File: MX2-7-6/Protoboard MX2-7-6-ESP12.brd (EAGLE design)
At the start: 54.2 x 59.6 mm, 248 parts

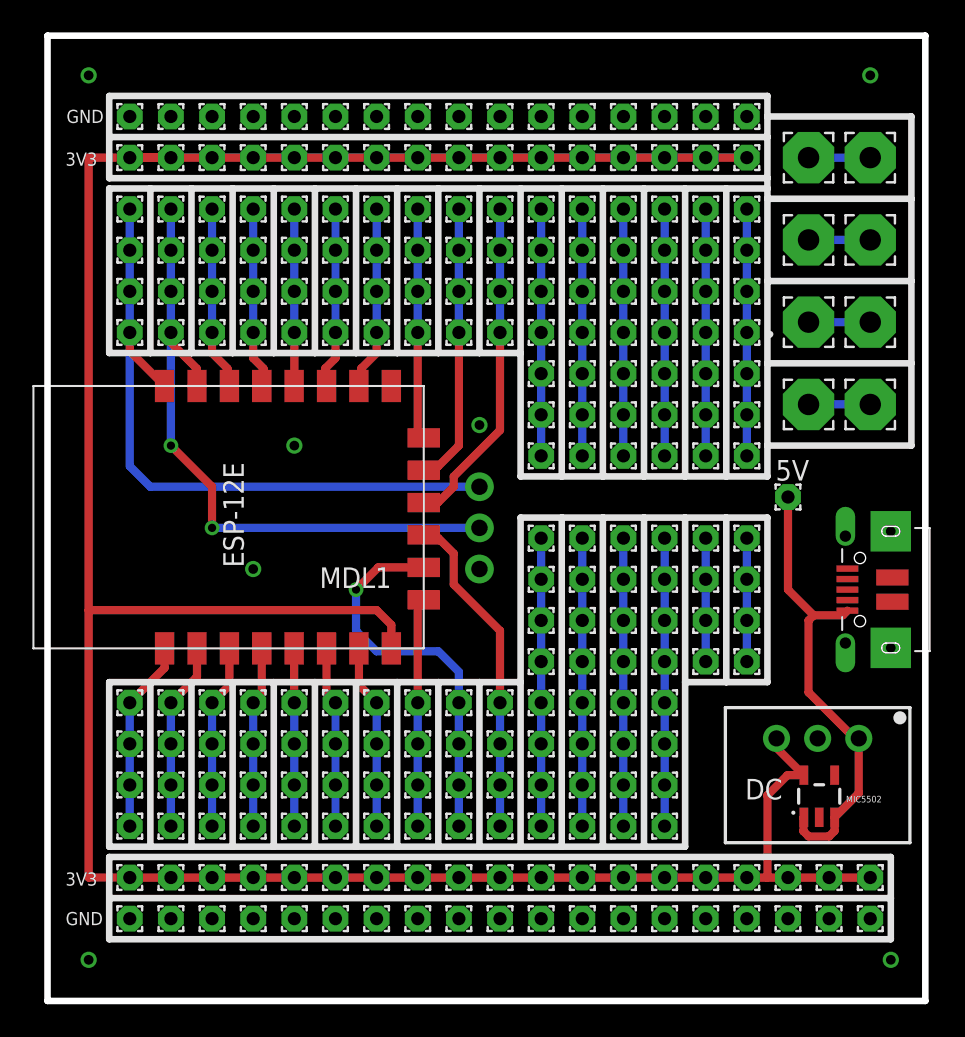
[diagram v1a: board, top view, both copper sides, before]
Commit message: Update to rev2
Updated to Pin headers instead of single wire pads
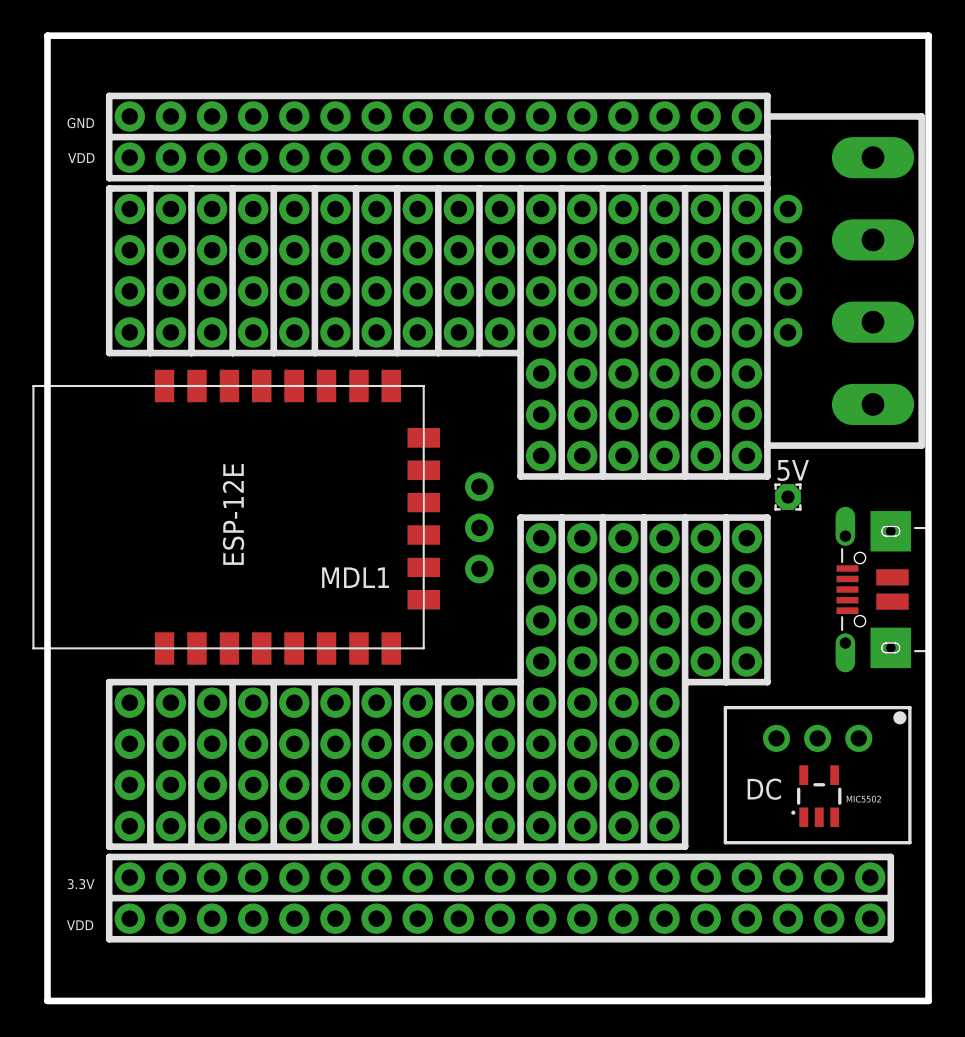
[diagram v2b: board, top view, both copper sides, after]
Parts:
- removed PAD10, PAD101, PAD102, PAD104, PAD105, PAD106, PAD107, PAD108, PAD11, PAD110, PAD112, PAD113, PAD114, PAD115, PAD116, PAD117, PAD12, PAD124, PAD125, PAD126, PAD13, PAD133, PAD134, PAD135, PAD14, PAD142, PAD143, PAD144, PAD15, PAD16, PAD169, PAD17, PAD170, PAD171, PAD172, PAD173, PAD174, PAD175, PAD178, PAD179, PAD18, PAD180, PAD181, PAD182, PAD183, PAD184, PAD187, PAD188, PAD189, PAD19, PAD190, PAD191, PAD192, PAD193, PAD196, PAD197, PAD198, PAD199, PAD20, PAD200, PAD201, PAD202, PAD205, PAD206, PAD207, PAD208, PAD209, PAD21, PAD210, PAD211, PAD214, PAD215, PAD216, PAD217, PAD218, PAD219, PAD22, PAD220, PAD23, PAD24, PAD25, PAD26, PAD269, PAD27, PAD270, PAD271, PAD272, PAD278, PAD279, PAD28, PAD280, PAD281, PAD282, PAD283, PAD284, PAD287, PAD288, PAD289, PAD29, PAD290, PAD291, PAD292, PAD293, PAD296, PAD297, PAD298, PAD299, PAD3, PAD30, PAD300, PAD301, PAD302, PAD305, PAD306, PAD307, PAD308, PAD309, PAD31, PAD310, PAD311, PAD32, PAD33, PAD36, PAD37, PAD38, PAD4, PAD41, PAD421, PAD422, PAD423, PAD424, PAD425, PAD426, PAD427, PAD428, PAD429, PAD430, PAD431, PAD432, PAD433, PAD434, PAD435, PAD436, PAD439, PAD44, PAD440, PAD441, PAD442, PAD443, PAD444, PAD445, PAD446, PAD447, PAD448, PAD449, PAD450, PAD451, PAD452, PAD453, PAD454, PAD455, PAD456, PAD459, PAD460, PAD461, PAD462, PAD48, PAD49, PAD5, PAD50, PAD52, PAD53, PAD54, PAD56, PAD57, PAD58, PAD6, PAD60, PAD61, PAD62, PAD64, PAD65, PAD66, PAD68, PAD69, PAD7, PAD70, PAD71, PAD72, PAD73, PAD74, PAD76, PAD77, PAD78, PAD79, PAD8, PAD80, PAD81, PAD83, PAD84, PAD85, PAD87, PAD88, PAD89, PAD9, PAD90, PAD92, PAD93, PAD96, PAD97, PAD98, PAD99: (no value), wirepad:1,6/0,8
- removed PAD100: 5, wirepad:1,6/0,8
- removed PAD103: SO, wirepad:1,6/0,8
- removed PAD109: 4, wirepad:1,6/0,8
- removed PAD111: 9, wirepad:1,6/0,8
- removed PAD118: 0, wirepad:1,6/0,8
- removed PAD127: 2, wirepad:1,6/0,8
- removed PAD136: 15, wirepad:1,6/0,8
- removed PAD145: SC, wirepad:1,6/0,8
- removed PAD34, PAD35, PAD39, PAD40, PAD42, PAD43, PAD45, PAD46: (no value), wirepad:3,17/1,3
- removed PAD47: AC, wirepad:1,6/0,8
- removed PAD51: CH, wirepad:1,6/0,8
- removed PAD55: 16, wirepad:1,6/0,8
- removed PAD59: 14, wirepad:1,6/0,8
- removed PAD63: 12, wirepad:1,6/0,8
- removed PAD67: 13, wirepad:1,6/0,8
- removed PAD75: CS, wirepad:1,6/0,8
- removed PAD82: TX, wirepad:1,6/0,8
- removed PAD86: SI, wirepad:1,6/0,8
- removed PAD91: RX, wirepad:1,6/0,8
- removed PAD94: 10, wirepad:1,6/0,8
- removed PAD95: RS, wirepad:1,6/0,8
- added 3.3V, VDD: (no value), SparkFun-Connectors:1X19_NO_SILK
- added GND, J33: (no value), SparkFun-Connectors:1X16_NO_SILK
- added J1, J10, J11, J12, J13, J14, J15, J16, J17, J18, J19, J2, J20, J3, J31, J32, J4, J5, J6, J7, J8, J9: (no value), SparkFun-Connectors:1X04_NO_SILK_ALL_ROUND
- added J21, J22, J23, J24, J25, J26: (no value), SparkFun-Connectors:1X07_NO_SILK
- added J27, J28, J29, J30: (no value), SparkFun-Connectors:1X08_NO_SILK
- added JP1, JP2, JP6, JP7: (no value), adafruit:1X1-BIGPOGO
- added JP10, JP11, JP8, JP9: (no value), adafruit:1X01-CLEANBIG
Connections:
- removed net N$2: PAD34.1, PAD35.1
- removed net N$38: MDL1.21, PAD83.1, PAD84.1, PAD85.1, PAD86.1
- removed net N$39: MDL1.20, PAD87.1, PAD92.1, PAD93.1, PAD94.1
- removed net N$4: PAD39.1, PAD40.1
- removed net N$42: MDL1.19, PAD111.1, PAD112.1, PAD113.1, PAD114.1
- removed net N$5: PAD42.1, PAD43.1
- removed net N$53: MDL1.4, PAD55.1, PAD56.1, PAD57.1, PAD58.1
- removed net N$58: MDL1.18, PAD103.1, PAD104.1, PAD105.1, PAD110.1
- removed net N$6: PAD45.1, PAD46.1
- new net N$15: J10.1, J10.2, J10.3, J10.4
- new net N$16: J18.1, J18.2, J18.3, J18.4
- new net N$23: J19.1, J19.2, J19.3, J19.4
- new net N$24: J20.1, J20.2, J20.3, J20.4
- new net N$25: J28.1, J28.2, J28.3, J28.4, J28.5, J28.6, J28.7, J28.8
- new net N$27: J29.1, J29.2, J29.3, J29.4, J29.5, J29.6, J29.7, J29.8
- new net N$3: J8.1, J8.2, J8.3, J8.4
- new net N$33: JP10.1, JP6.P$1
- new net N$34: J17.1, J17.2, J17.3, J17.4
- new net N$7: J1.1, J1.2, J1.3, J1.4
- new net N$8: J2.1, J2.2, J2.3, J2.4
- net GND: now also GND.1, GND.10, GND.11, GND.12, GND.13, GND.14, GND.15, GND.16, GND.2, GND.3, GND.4, GND.5, GND.6, GND.7, GND.8, GND.9, VDD.1, VDD.10, VDD.11, VDD.12, VDD.13, VDD.14, VDD.15, VDD.16, VDD.17, VDD.18, VDD.19, VDD.2, VDD.3, VDD.4, VDD.5, VDD.6, VDD.7, VDD.8, VDD.9; no longer PAD17.1, PAD22.1, PAD23.1, PAD24.1, PAD25.1, PAD26.1, PAD27.1, PAD28.1, PAD29.1, PAD30.1, PAD31.1, PAD32.1, PAD33.1, PAD36.1, PAD38.1, PAD4.1, PAD421.1, PAD422.1, PAD423.1, PAD424.1, PAD425.1, PAD426.1, PAD427.1, PAD428.1, PAD429.1, PAD430.1, PAD431.1, PAD432.1, PAD433.1, PAD434.1, PAD435.1, PAD436.1, PAD439.1, PAD440.1, PAD441.1
- net N$1: now also J21.1, J21.2, J21.3, J21.4, J21.5, J21.6, J21.7; no longer PAD3.1, PAD37.1, PAD41.1, PAD44.1
- net N$10: now also J4.1, J4.2, J4.3, J4.4; no longer PAD106.1, PAD107.1, PAD108.1, PAD109.1
- net N$11: now also J5.1, J5.2, J5.3, J5.4; no longer PAD115.1, PAD116.1, PAD117.1, PAD118.1
- net N$12: now also J6.1, J6.2, J6.3, J6.4; no longer PAD124.1, PAD125.1, PAD126.1, PAD127.1
- net N$13: now also J7.1, J7.2, J7.3, J7.4; no longer PAD133.1, PAD134.1, PAD135.1, PAD136.1
- net N$14: now also J9.1, J9.2, J9.3, J9.4; no longer MDL1.22, PAD142.1, PAD143.1, PAD144.1, PAD145.1
- net N$17: now also J22.1, J22.2, J22.3, J22.4, J22.5, J22.6, J22.7; no longer PAD169.1, PAD170.1, PAD171.1, PAD172.1, PAD173.1, PAD174.1, PAD175.1
- net N$18: now also J23.1, J23.2, J23.3, J23.4, J23.5, J23.6, J23.7; no longer PAD178.1, PAD179.1, PAD180.1, PAD181.1, PAD182.1, PAD183.1, PAD184.1
- net N$19: now also J24.1, J24.2, J24.3, J24.4, J24.5, J24.6, J24.7; no longer PAD187.1, PAD188.1, PAD189.1, PAD190.1, PAD191.1, PAD192.1, PAD193.1
- net N$20: now also J25.1, J25.2, J25.3, J25.4, J25.5, J25.6, J25.7; no longer PAD196.1, PAD197.1, PAD198.1, PAD199.1, PAD200.1, PAD201.1, PAD202.1
- net N$21: now also J26.1, J26.2, J26.3, J26.4, J26.5, J26.6, J26.7; no longer PAD205.1, PAD206.1, PAD207.1, PAD208.1, PAD209.1, PAD210.1, PAD211.1
- net N$22: now also J27.1, J27.2, J27.3, J27.4, J27.5, J27.6, J27.7, J27.8; no longer PAD214.1, PAD215.1, PAD216.1, PAD217.1, PAD218.1, PAD219.1, PAD220.1
- net N$26: now also J14.1, J14.2, J14.3, J14.4; no longer PAD59.1, PAD60.1, PAD61.1, PAD62.1
- net N$28: now also J30.1, J30.2, J30.3, J30.4, J30.5, J30.6, J30.7, J30.8; no longer PAD269.1, PAD270.1, PAD271.1, PAD272.1
- net N$29: now also J31.1, J31.2, J31.3, J31.4; no longer PAD278.1, PAD279.1, PAD280.1, PAD281.1, PAD282.1, PAD283.1, PAD284.1, PAD71.1
- net N$30: now also J32.1, J32.2, J32.3, J32.4; no longer PAD287.1, PAD288.1, PAD289.1, PAD290.1, PAD291.1, PAD292.1, PAD293.1, PAD72.1
- net N$31: now also JP1.P$1, JP8.1; no longer PAD296.1, PAD297.1, PAD298.1, PAD299.1, PAD300.1, PAD301.1, PAD302.1, PAD73.1
- net N$32: now also JP2.P$1, JP9.1; no longer PAD305.1, PAD306.1, PAD307.1, PAD308.1, PAD309.1, PAD310.1, PAD311.1, PAD74.1
- net N$35: now also JP11.1, JP7.P$1; no longer MDL1.17, PAD75.1, PAD76.1, PAD77.1, PAD78.1
- net N$50: now also J11.1, J11.2, J11.3, J11.4; no longer PAD101.1, PAD102.1, PAD95.1, PAD96.1
- net N$51: now also J12.1, J12.2, J12.3, J12.4; no longer PAD47.1, PAD48.1, PAD49.1, PAD50.1
- net N$52: now also J13.1, J13.2, J13.3, J13.4; no longer PAD51.1, PAD52.1, PAD53.1, PAD54.1
- net N$55: now also J15.1, J15.2, J15.3, J15.4; no longer PAD63.1, PAD64.1, PAD65.1, PAD66.1
- net N$56: now also J16.1, J16.2, J16.3, J16.4; no longer PAD67.1, PAD68.1, PAD69.1, PAD70.1
- net N$9: now also J3.1, J3.2, J3.3, J3.4; no longer PAD100.1, PAD97.1, PAD98.1, PAD99.1
- net RX: no longer PAD88.1, PAD89.1, PAD90.1, PAD91.1
- net TX: no longer PAD79.1, PAD80.1, PAD81.1, PAD82.1
- net VDD: now also 3.3V.1, 3.3V.10, 3.3V.11, 3.3V.12, 3.3V.13, 3.3V.14, 3.3V.15, 3.3V.16, 3.3V.17, 3.3V.18, 3.3V.19, 3.3V.2, 3.3V.3, 3.3V.4, 3.3V.5, 3.3V.6, 3.3V.7, 3.3V.8, 3.3V.9, J33.1, J33.10, J33.11, J33.12, J33.13, J33.14, J33.15, J33.16, J33.2, J33.3, J33.4, J33.5, J33.6, J33.7, J33.8, J33.9; no longer PAD10.1, PAD11.1, PAD12.1, PAD13.1, PAD14.1, PAD15.1, PAD16.1, PAD18.1, PAD19.1, PAD20.1, PAD21.1, PAD442.1, PAD443.1, PAD444.1, PAD445.1, PAD446.1, PAD447.1, PAD448.1, PAD449.1, PAD450.1, PAD451.1, PAD452.1, PAD453.1, PAD454.1, PAD455.1, PAD456.1, PAD459.1, PAD460.1, PAD461.1, PAD462.1, PAD5.1, PAD6.1, PAD7.1, PAD8.1, PAD9.1
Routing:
- net VDD: track 263.6 -> 0.00 mm
- net TX: track 42.8 -> 0.00 mm
- net RX: track 42.2 -> 0.00 mm, vias 2 -> 0
- net VCC: track 28.7 -> 0.00 mm
- net N$58: track 25.2 -> 0.00 mm, vias 1 -> 0
- net N$39: track 21.4 -> 0.00 mm
- net N$42: track 21.2 -> 0.00 mm
- net N$29: track 19.6 -> 0.00 mm
- net N$32: track 19.2 -> 0.00 mm
- net N$30: track 19.2 -> 0.00 mm
- net N$38: track 18.4 -> 0.00 mm
- net N$31: track 17.8 -> 0.00 mm
- net N$21: track 17.7 -> 0.00 mm
- net N$18: track 16.9 -> 0.00 mm
- net N$22: track 16.9 -> 0.00 mm
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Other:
- board size 54.2 x 59.6 mm -> 54.4 x 59.6 mm
- board text added: "VDD"
- board text removed: "3V3"
- board text removed: "GND"

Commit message: Change usb connector
Change to correct usb connecter and moved esp8266 bit more onto the
board.
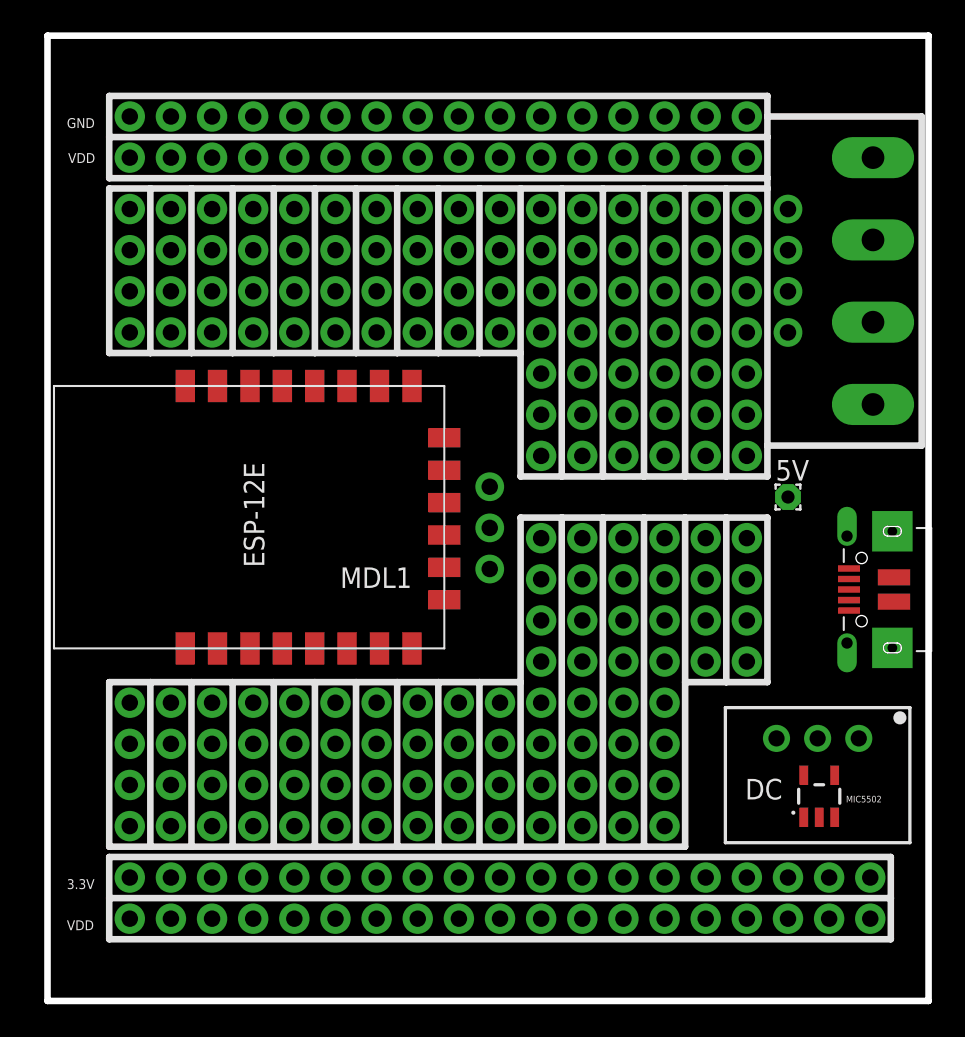
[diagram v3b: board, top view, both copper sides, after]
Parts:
- moved MDL1 1.27 mm to (14.3, 29.4)
- moved JP3 0.63 mm to (27.3, 31.8)
- moved JP4 0.63 mm to (27.3, 29.2)
- moved JP5 0.63 mm to (27.3, 26.7)
- moved X2 0.10 mm to (50.3, 25.4)
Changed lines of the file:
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@@
 <attribute name="NAME" x="43.0758625" y="12.441459375" size="1.27" layer="25"/>
 </element>
-<element name="JP3" library="adafruit" package="1X01-CLEANBIG" value="TX" x="26.67" y="31.75" smashed="yes">
-<attribute name="VALUE" x="28.57" y="31.205" size="0.6096" layer="27" rot="R90"/>
-</element>
-<element name="JP4" library="adafruit" package="1X01-CLEANBIG" value="RX" x="26.67" y="29.21" smashed="yes">
-<attribute name="VALUE" x="28.55" y="28.765" size="0.6096" layer="27" rot="R90"/>
-</element>
-<element name="JP5" library="adafruit" package="1X01-CLEANBIG" value="GND" x="26.67" y="26.67" smashed="yes">
-<attribute name="VALUE" x="28.58" y="25.775" size="0.6096" layer="27" rot="R90"/>
-</element>
-<element name="X2" library="microbuilder" package="4UCONN_20329" value="" x="50.165" y="25.4" smashed="yes" rot="R90">
-<attribute name="VALUE" x="56.575" y="22.622" size="0.4064" layer="27" ratio="10" rot="R90"/>
-</element>
-<element name="MDL1" library="ESP8266-ESP12E" package="ESP8266-ESP12E" value="" x="13.07" y="29.39" smashed="yes" rot="R90">
-<attribute name="NAME" x="21.23" y="26.77" size="1.27" layer="21" rot="R180"/>
+<element name="JP3" library="adafruit" package="1X01-CLEANBIG" value="TX" x="27.305" y="31.75" smashed="yes">
+<attribute name="VALUE" x="28.57" y="30.57" size="0.3048" layer="27" rot="R90"/>
+</element>
+<element name="JP4" library="adafruit" package="1X01-CLEANBIG" value="RX" x="27.305" y="29.21" smashed="yes">
+<attribute name="VALUE" x="28.55" y="28.13" size="0.3048" layer="27" rot="R90"/>
+</element>
+<element name="JP5" library="adafruit" package="1X01-CLEANBIG" value="GND" x="27.305" y="26.67" smashed="yes">
+<attribute name="VALUE" x="28.58" y="25.14" size="0.3048" layer="27" rot="R90"/>
+</element>
+<element name="X2" library="microbuilder" package="4UCONN_20329" value="" x="50.265" y="25.4" smashed="yes" rot="R90">
+<attribute name="VALUE" x="56.675" y="22.622" size="0.4064" layer="27" ratio="10" rot="R90"/>
+</element>
+<element name="MDL1" library="ESP8266-ESP12E" package="ESP8266-ESP12E" value="" x="14.34" y="29.39" smashed="yes" rot="R90">
+<attribute name="NAME" x="22.5" y="26.77" size="1.27" layer="21" rot="R180"/>
 </element>
 <element name="MIC5502" library="SparkFun-PowerIC" package="SOT23-5" value="" x="47.65" y="12.64" smashed="yes">
@@
 <wire x1="5.08" y1="43.815" x2="5.08" y2="46.355" width="0" layer="19" extent="1-1"/>
 <wire x1="5.08" y1="41.275" x2="5.08" y2="43.815" width="0" layer="19" extent="1-1"/>
-<wire x1="11.23" y1="37.97" x2="5.08" y2="41.275" width="0" layer="19" extent="1-1"/>
+<wire x1="12.5" y1="37.97" x2="5.08" y2="41.275" width="0" layer="19" extent="1-1"/>
 </signal>
 <signal name="N$10">
@@
 <wire x1="7.62" y1="43.815" x2="7.62" y2="46.355" width="0" layer="19" extent="1-1"/>
 <wire x1="7.62" y1="41.275" x2="7.62" y2="43.815" width="0" layer="19" extent="1-1"/>
-<wire x1="13.23" y1="37.97" x2="7.62" y2="41.275" width="0" layer="19" extent="1-1"/>
+<wire x1="14.5" y1="37.97" x2="7.62" y2="41.275" width="0" layer="19" extent="1-1"/>
 </signal>
 <signal name="N$11">
@@
 <wire x1="10.16" y1="43.815" x2="10.16" y2="46.355" width="0" layer="19" extent="1-1"/>
 <wire x1="10.16" y1="41.275" x2="10.16" y2="43.815" width="0" layer="19" extent="1-1"/>
-<wire x1="15.23" y1="37.97" x2="10.16" y2="41.275" width="0" layer="19" extent="1-1"/>
+<wire x1="16.5" y1="37.97" x2="10.16" y2="41.275" width="0" layer="19" extent="1-1"/>
 </signal>
 <signal name="N$12">
@@
 <wire x1="12.7" y1="43.815" x2="12.7" y2="46.355" width="0" layer="19" extent="1-1"/>
 <wire x1="12.7" y1="41.275" x2="12.7" y2="43.815" width="0" layer="19" extent="1-1"/>
-<wire x1="17.23" y1="37.97" x2="12.7" y2="41.275" width="0" layer="19" extent="1-1"/>
+<wire x1="18.5" y1="37.97" x2="12.7" y2="41.275" width="0" layer="19" extent="1-1"/>
 </signal>
 <signal name="N$13">
@@
 <wire x1="15.24" y1="43.815" x2="15.24" y2="46.355" width="0" layer="19" extent="1-1"/>
 <wire x1="15.24" y1="41.275" x2="15.24" y2="43.815" width="0" layer="19" extent="1-1"/>
-<wire x1="19.23" y1="37.97" x2="15.24" y2="41.275" width="0" layer="19" extent="1-1"/>
+<wire x1="20.5" y1="37.97" x2="15.24" y2="41.275" width="0" layer="19" extent="1-1"/>
 </signal>
 <signal name="GND">
@@
 <contactref element="MIC5502" pad="3"/>
 <contactref element="5V" pad="1"/>
-<wire x1="49.39" y1="24.1" x2="45.72" y2="31.115" width="0" layer="19" extent="1-1"/>
-<wire x1="50.0908625" y1="16.211459375" x2="49.39" y2="24.1" width="0" layer="19" extent="1-1"/>
+<wire x1="49.49" y1="24.1" x2="45.72" y2="31.115" width="0" layer="19" extent="1-1"/>
+<wire x1="50.0908625" y1="16.211459375" x2="49.49" y2="24.1" width="0" layer="19" extent="1-1"/>
 <wire x1="48.6" y1="11.3399" x2="50.0908625" y2="16.211459375" width="0" layer="19" extent="1-1"/>
 <wire x1="46.7" y1="11.3399" x2="48.6" y2="11.3399" width="0" layer="19" extent="1-1"/>
@@
 <wire x1="7.62" y1="52.07" x2="10.16" y2="52.07" width="0" layer="19" extent="1-1"/>
 <wire x1="5.08" y1="52.07" x2="7.62" y2="52.07" width="0" layer="19" extent="1-1"/>
-<wire x1="21.23" y1="21.77" x2="20.32" y2="52.07" width="0" layer="19" extent="1-1"/>
-<wire x1="20.32" y1="7.62" x2="21.23" y2="21.77" width="0" layer="19" extent="1-1"/>
+<wire x1="22.5" y1="21.77" x2="20.32" y2="52.07" width="0" layer="19" extent="1-1"/>
+<wire x1="20.32" y1="7.62" x2="22.5" y2="21.77" width="0" layer="19" extent="1-1"/>
 <wire x1="22.86" y1="7.62" x2="20.32" y2="7.62" width="0" layer="19" extent="1-1"/>
 <wire x1="25.4" y1="7.62" x2="22.86" y2="7.62" width="0" layer="19" extent="1-1"/>
@@
 <contactref element="J14" pad="2"/>
 <contactref element="J14" pad="1"/>
-<wire x1="12.7" y1="18.415" x2="15.23" y2="21.77" width="0" layer="19" extent="1-1"/>
+<wire x1="12.7" y1="18.415" x2="16.5" y2="21.77" width="0" layer="19" extent="1-1"/>
 <wire x1="12.7" y1="15.875" x2="12.7" y2="18.415" width="0" layer="19" extent="1-1"/>
 <wire x1="12.7" y1="13.335" x2="12.7" y2="15.875" width="0" layer="19" extent="1-1"/>
@@
 <contactref element="J11" pad="2"/>
 <contactref element="J11" pad="1"/>
-<wire x1="5.08" y1="18.415" x2="7.23" y2="21.77" width="0" layer="19" extent="1-1"/>
+<wire x1="5.08" y1="18.415" x2="8.5" y2="21.77" width="0" layer="19" extent="1-1"/>
 <wire x1="5.08" y1="15.875" x2="5.08" y2="18.415" width="0" layer="19" extent="1-1"/>
 <wire x1="5.08" y1="13.335" x2="5.08" y2="15.875" width="0" layer="19" extent="1-1"/>
@@
 <contactref element="J12" pad="2"/>
 <contactref element="J12" pad="1"/>
-<wire x1="7.62" y1="18.415" x2="9.23" y2="21.77" width="0" layer="19" extent="1-1"/>
+<wire x1="7.62" y1="18.415" x2="10.5" y2="21.77" width="0" layer="19" extent="1-1"/>
 <wire x1="7.62" y1="15.875" x2="7.62" y2="18.415" width="0" layer="19" extent="1-1"/>
 <wire x1="7.62" y1="13.335" x2="7.62" y2="15.875" width="0" layer="19" extent="1-1"/>
@@
 <contactref element="J13" pad="2"/>
 <contactref element="J13" pad="1"/>
-<wire x1="10.16" y1="18.415" x2="11.23" y2="21.77" width="0" layer="19" extent="1-1"/>
+<wire x1="10.16" y1="18.415" x2="12.5" y2="21.77" width="0" layer="19" extent="1-1"/>
 <wire x1="10.16" y1="15.875" x2="10.16" y2="18.415" width="0" layer="19" extent="1-1"/>
 <wire x1="10.16" y1="13.335" x2="10.16" y2="15.875" width="0" layer="19" extent="1-1"/>
@@
 <contactref element="J15" pad="3"/>
 <contactref element="J15" pad="4"/>
-<wire x1="15.24" y1="18.415" x2="17.23" y2="21.77" width="0" layer="19" extent="1-1"/>
+<wire x1="15.24" y1="18.415" x2="18.5" y2="21.77" width="0" layer="19" extent="1-1"/>
 <wire x1="15.24" y1="15.875" x2="15.24" y2="18.415" width="0" layer="19" extent="1-1"/>
 <wire x1="15.24" y1="13.335" x2="15.24" y2="15.875" width="0" layer="19" extent="1-1"/>
@@
 <contactref element="J16" pad="3"/>
 <contactref element="J16" pad="4"/>
-<wire x1="17.78" y1="18.415" x2="19.23" y2="21.77" width="0" layer="19" extent="1-1"/>
+<wire x1="17.78" y1="18.415" x2="20.5" y2="21.77" width="0" layer="19" extent="1-1"/>
 <wire x1="17.78" y1="15.875" x2="17.78" y2="18.415" width="0" layer="19" extent="1-1"/>
 <wire x1="17.78" y1="13.335" x2="17.78" y2="15.875" width="0" layer="19" extent="1-1"/>
@@
 <contactref element="MDL1" pad="16"/>
 <contactref element="JP3" pad="1"/>
-<wire x1="7.23" y1="37.97" x2="26.67" y2="31.75" width="0" layer="19" extent="1-1"/>
+<wire x1="8.5" y1="37.97" x2="27.305" y2="31.75" width="0" layer="19" extent="1-1"/>
 </signal>
 <signal name="RX">
 <contactref element="MDL1" pad="15"/>
 <contactref element="JP4" pad="1"/>
-<wire x1="9.23" y1="37.97" x2="26.67" y2="29.21" width="0" layer="19" extent="1-1"/>
+<wire x1="10.5" y1="37.97" x2="27.305" y2="29.21" width="0" layer="19" extent="1-1"/>
 </signal>
 <signal name="N$3">

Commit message: Change ESP Module
Changed to Device/Package Adafruit uses
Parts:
- removed MDL1: (no value), ESP8266-ESP12E:ESP8266-ESP12E
- added X1: ESP-12E, microbuilder:ESP-12E
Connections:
- removed net N$26: J14.1, J14.2, J14.3, J14.4, MDL1.5
- removed net N$55: J15.1, J15.2, J15.3, J15.4, MDL1.6
- removed net N$56: J16.1, J16.2, J16.3, J16.4, MDL1.7
- new net N$2: J16.1, J16.2, J16.3, J16.4, X1.6
- new net N$36: J14.1, J14.2, J14.3, J14.4, X1.4
- new net N$6: J15.1, J15.2, J15.3, J15.4, X1.5
- net GND: now also X1.9; no longer MDL1.9
- net N$10: now also X1.13; no longer MDL1.13
- net N$11: now also X1.12; no longer MDL1.12
- net N$12: now also X1.11; no longer MDL1.11
- net N$13: now also X1.10; no longer MDL1.10
- net N$34: now also X1.7
- net N$50: now also X1.1; no longer MDL1.1
- net N$51: now also X1.2; no longer MDL1.2
- net N$52: now also X1.3; no longer MDL1.3
- net N$9: now also X1.14; no longer MDL1.14
- net RX: now also X1.15; no longer MDL1.15
- net TX: now also X1.16; no longer MDL1.16
- net VDD: now also X1.8; no longer MDL1.8

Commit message: Update esp component and usb
test
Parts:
- moved 5V 2.54 mm to (45.7, 28.6)
- moved JP1 1.91 mm to (51.0, 50.2)
- moved JP10 1.91 mm to (45.7, 41.9)
- moved JP11 1.91 mm to (45.7, 39.4)
- moved JP2 1.91 mm to (51.0, 45.1)
- moved JP7 1.91 mm to (51.0, 34.9)
- moved JP8 1.91 mm to (45.7, 47.0)
- moved JP6 1.90 mm to (51.0, 40.0)
- moved JP9 1.90 mm to (45.7, 44.5)
- moved X1 0.63 mm to (15.2, 29.8)
